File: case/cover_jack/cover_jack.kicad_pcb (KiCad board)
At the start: 2 copper layers, 14 x 36.2 mm, 0 parts

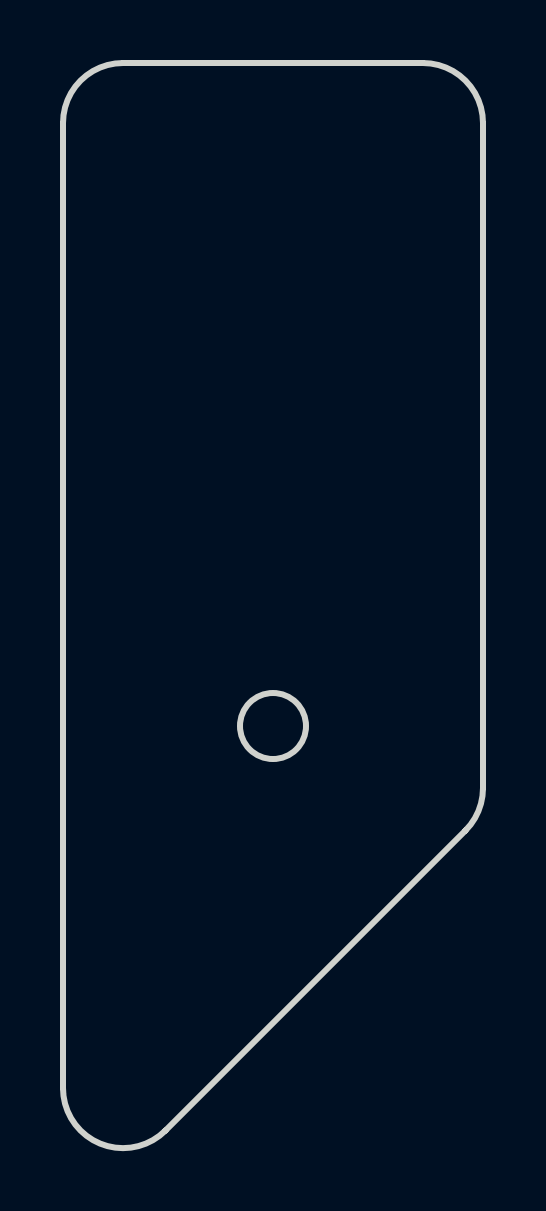
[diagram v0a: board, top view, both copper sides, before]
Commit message: Circles to holes
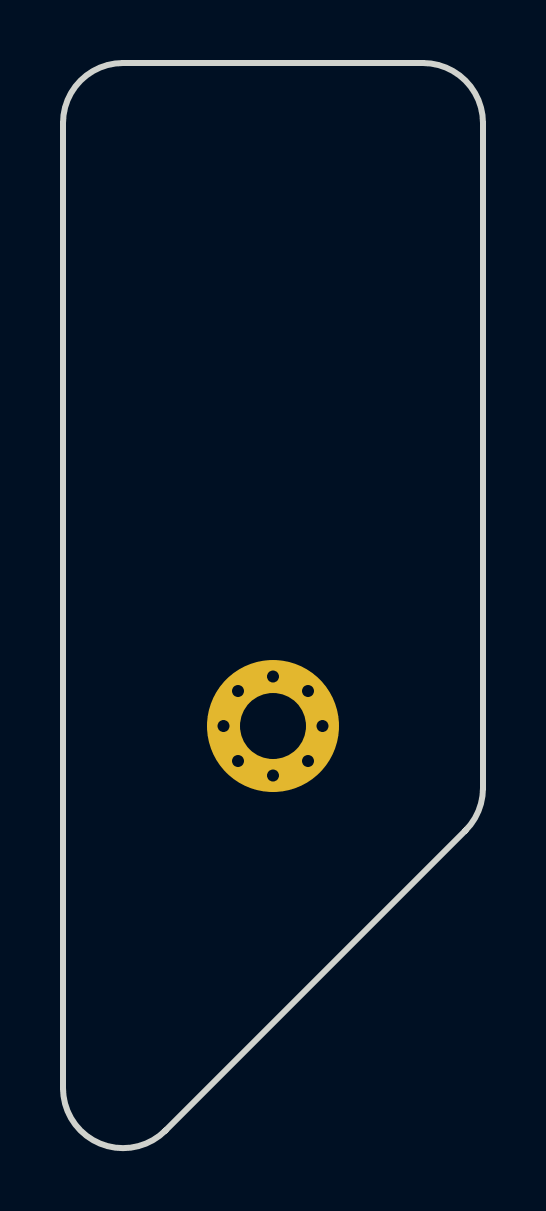
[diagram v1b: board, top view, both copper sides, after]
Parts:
- added REF**: MountingHole_2.2mm_M2_Pad_Via, MountingHole_2.2mm_M2_Pad_Via, F.Cu at (215.2, 59.1)
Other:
- outline, holes or cut-outs redrawn
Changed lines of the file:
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@@
     (tracks 0)
     (zones 0)
-    (modules 0)
+    (modules 1)
     (nets 1)
   )
@@
     (uvia_drill 0.1)
   )
-  (gr_circle (center 215.25 59.100505) (end 216.35 59.100505) (layer Edge.Cuts) (width 0.2))
+  (module MountingHole_2.2mm_M2_Pad_Via (layer F.Cu)
+    (at 215.25 59.100505)
+    (descr "Mounting Hole 2.2mm, M2")
+    (tags "mounting hole 2.2mm m2")
+    (attr virtual)
+    (fp_text reference REF** (at 0 -3.2) (layer F.SilkS) hide
+      (effects (font (size 1 1) (thickness 0.15)))
+    )
+    (fp_text value MountingHole_2.2mm_M2_Pad_Via (at 0 3.2) (layer F.Fab)
+      (effects (font (size 1 1) (thickness 0.15)))
+    )
+    (fp_circle (center 0 0) (end 2.45 0) (layer F.CrtYd) (width 0.05))
+    (fp_circle (center 0 0) (end 2.2 0) (layer Cmts.User) (width 0.15))
+    (fp_text user %R (at 0.3 0) (layer F.Fab)
+      (effects (font (size 1 1) (thickness 0.15)))
+    )
+    (pad 1 thru_hole circle (at 1.166726 -1.166726) (size 0.7 0.7) (drill 0.4) (layers *.Cu *.Mask))
+    (pad 1 thru_hole circle (at 0 -1.65) (size 0.7 0.7) (drill 0.4) (layers *.Cu *.Mask))
+    (pad 1 thru_hole circle (at -1.166726 -1.166726) (size 0.7 0.7) (drill 0.4) (layers *.Cu *.Mask))
+    (pad 1 thru_hole circle (at -1.65 0) (size 0.7 0.7) (drill 0.4) (layers *.Cu *.Mask))
+    (pad 1 thru_hole circle (at -1.166726 1.166726) (size 0.7 0.7) (drill 0.4) (layers *.Cu *.Mask))
+    (pad 1 thru_hole circle (at 0 1.65) (size 0.7 0.7) (drill 0.4) (layers *.Cu *.Mask))
+    (pad 1 thru_hole circle (at 1.166726 1.166726) (size 0.7 0.7) (drill 0.4) (layers *.Cu *.Mask))
+    (pad 1 thru_hole circle (at 1.65 0) (size 0.7 0.7) (drill 0.4) (layers *.Cu *.Mask))
+    (pad 1 thru_hole circle (at 0 0) (size 4.4 4.4) (drill 2.2) (layers *.Cu *.Mask))
+  )
+  (gr_circle (center 215.25 59.100505) (end 216.35 59.100505) (layer Eco1.User) (width 0.2))
   (gr_arc (start 210.25 39) (end 210.25 37) (angle -90) (layer Edge.Cuts) (width 0.2))
   (gr_line (start 208.25 71.171572) (end 208.25 39) (layer Edge.Cuts) (width 0.2))
